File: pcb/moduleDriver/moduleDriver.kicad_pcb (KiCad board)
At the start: 2 copper layers, 72 x 80 mm, 56 parts, among them J1 MOTOR, J10 Sensor, J11 Power, J12 Power, J13 Power, J2 MOTOR, J3 MOTOR, J4 MOTOR, J5 IDC, J6 IDC, J7 Sensor, J8 Sensor, J9 Sensor, U1 TPIC6B595, U2 TPIC6B595, U3 74HC165, U4 74HC125, U5 PicoW, U6 OKI-78SR-5_1.5-W36-C, U8 74AHCT125

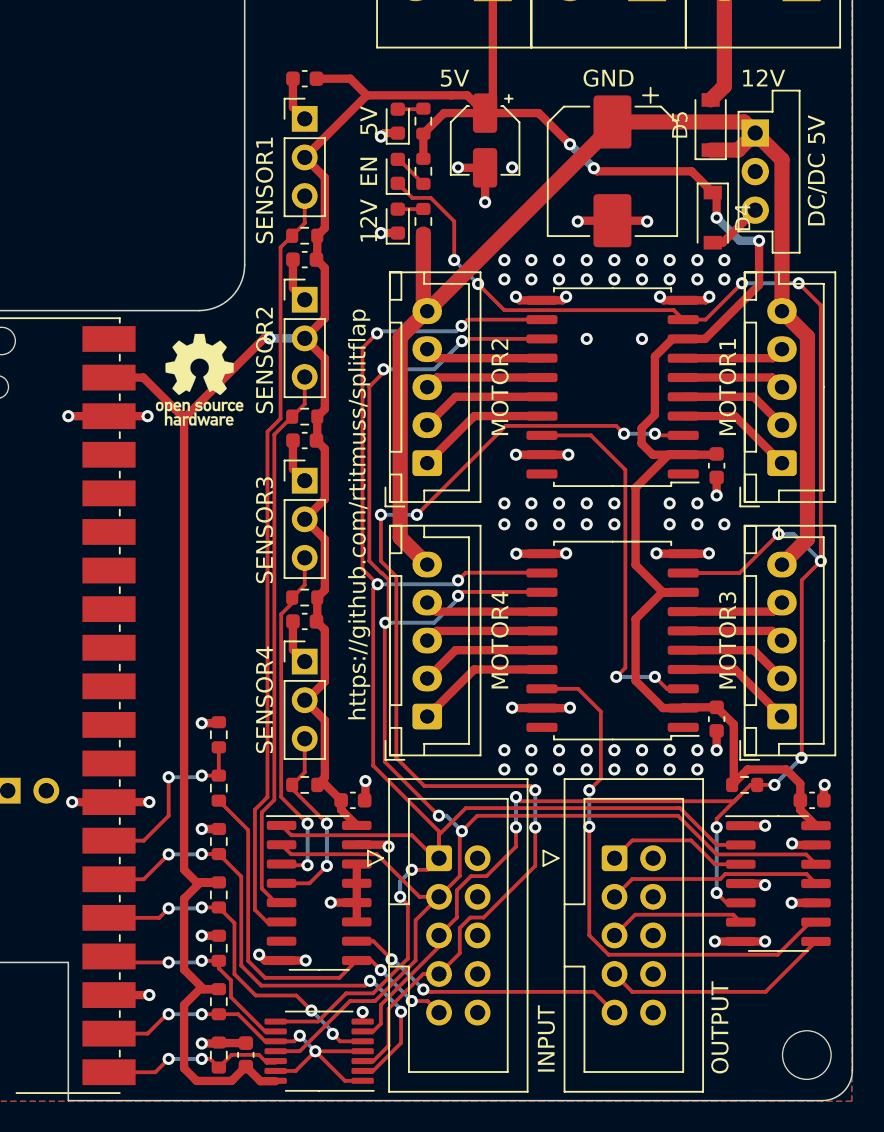
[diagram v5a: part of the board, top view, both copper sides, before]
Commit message: Iterate on level translation
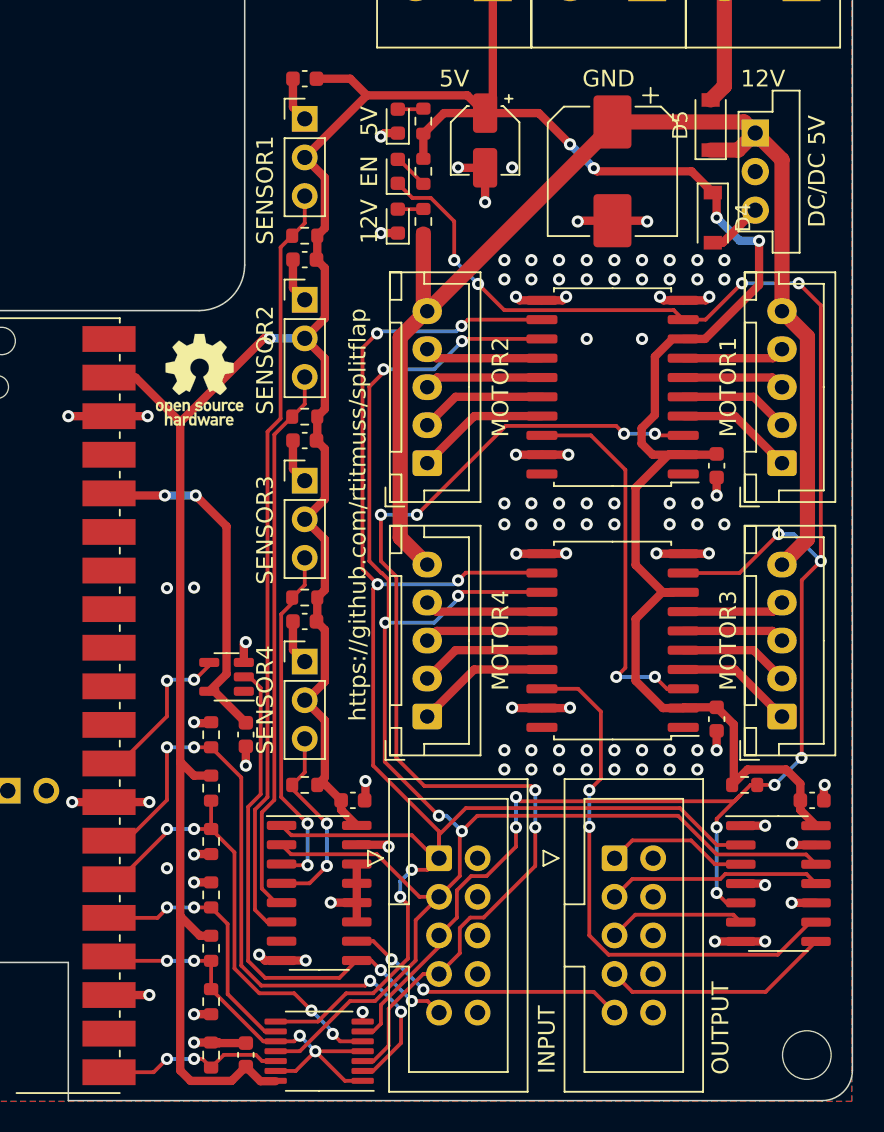
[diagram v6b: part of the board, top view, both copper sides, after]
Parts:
- removed R10: 2.4k, Resistor_SMD:R_0603_1608Metric
- removed R11: 1.2k, Resistor_SMD:R_0603_1608Metric
- added C8: 1uF, Capacitor_SMD:C_0603_1608Metric, F.Cu at (100.1, 105.9)
- added R16: 100k, Resistor_SMD:R_0603_1608Metric, F.Cu at (97.8, 112.9)
- added R17: 4.7k, Resistor_SMD:R_0603_1608Metric, F.Cu at (97.8, 123.5)
- added U7: SN74LVC1G04DBVR, Package_TO_SOT_SMD:SOT-23-5, F.Cu at (98.8, 102.1)
- R1: value 2.4k -> 2.2k
- R12, R9: value 100k -> 2.2k
- R15: value 100k -> 4.7k
- moved R15 17.6 mm to (97.8, 105.9), turned to -90 degrees
- moved R13 3.55 mm to (97.8, 116.5)
- moved R9 3.55 mm to (97.8, 120.0)
- moved R12 3.55 mm to (97.8, 109.4), turned to 90 degrees
- moved R4 0.51 mm to (97.8, 127.0)
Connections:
- R12 pad 1: GND -> /~{PWR_ENABLE_IN_3V3}
- R12 pad 2: /MOTOR_IN_3V3 -> +5V
- R15 pad 1: /~{BUFFER_ENABLE_3V3} -> GND
- R15 pad 2: +5V -> /MOTOR_IN_3V3
- R9 pad 1: /~{PWR_ENABLE_IN_3V3} -> /~{BUFFER_ENABLE_3V3}
- U5 pad 22: /~{BUFFER_ENABLE_3V3} -> unconnected-(U5-Pad22)
- U5 pad 24: /LATCH_IN_3V3 -> /~{BUFFER_ENABLE_3V3}
- U5 pad 25: /~{PWR_ENABLE_IN_3V3} -> /LATCH_IN_3V3
- U5 pad 26: /MOTOR_IN_3V3 -> /~{PWR_ENABLE_IN_3V3}
- U5 pad 27: /SENSOR_OUT_3V3 -> /MOTOR_IN_3V3
- U5 pad 29: unconnected-(U5-Pad29) -> /~{SENSOR_OUT_3V3}
- U5 pad 36: unconnected-(U5-Pad36) -> +3.3V
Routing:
- net +3.3V: track 0.00 -> 23.6 mm, vias 0 -> 2
- net /SENSOR_OUT_3V3: track 13.1 -> 0.00 mm, vias 2 -> 0
- net /~{SENSOR_OUT_3V3}: track 0.00 -> 10.1 mm, vias 0 -> 2
- net /MOTOR_IN_3V3: track 34.1 -> 42.6 mm
- net /SENSOR_OUT: track 26.3 -> 34.3 mm
- net /~{PWR_ENABLE_IN_3V3}: track 23.8 -> 29.8 mm
- net +5V: track 248.4 -> 244.4 mm
- net GND: track 108.5 -> 111.6 mm, vias 101 -> 107
- net /LATCH_IN_3V3: track 15.2 -> 18.3 mm
- net /~{BUFFER_ENABLE_3V3}: track 26.6 -> 28.3 mm
- net +12V: track 84.5 -> 83.8 mm

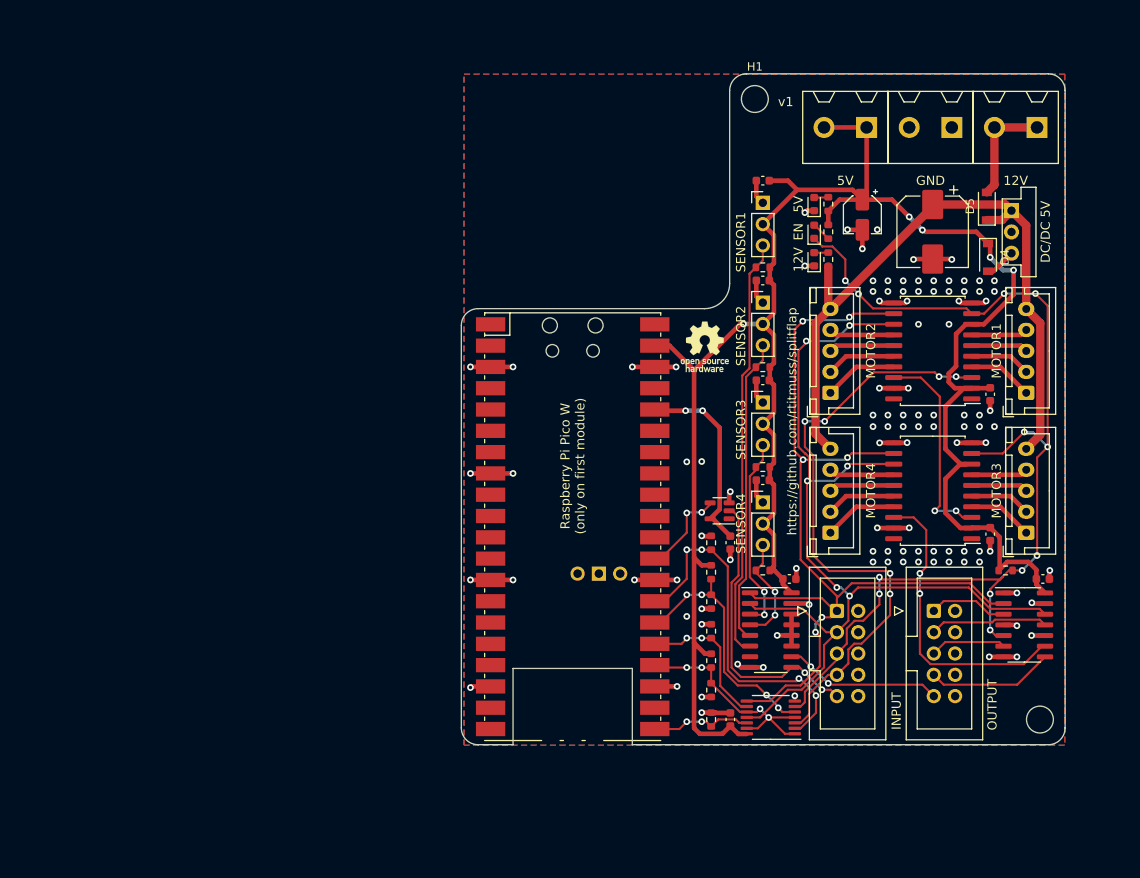
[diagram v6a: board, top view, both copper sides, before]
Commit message: Initial layout for new schematic
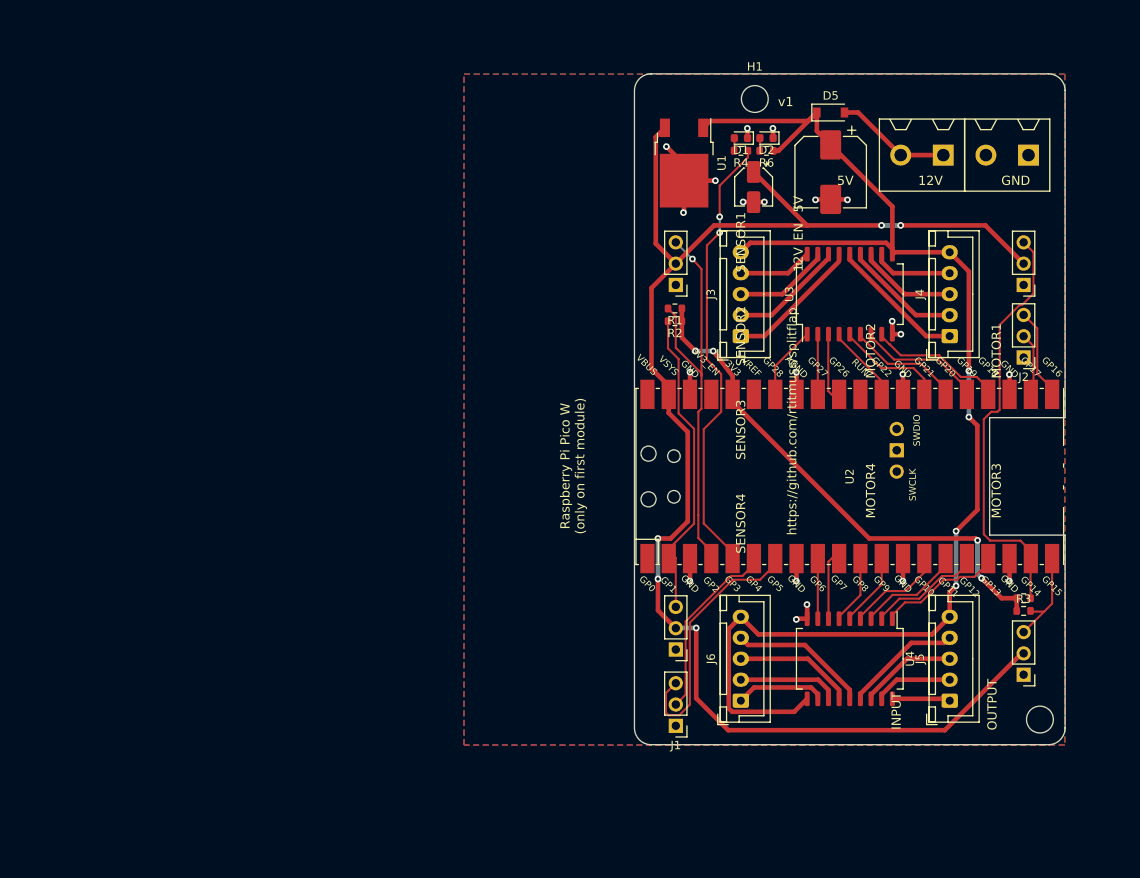
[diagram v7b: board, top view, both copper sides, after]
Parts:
- removed C10, C11, C12, C2, C3, C5, C6, C7, C8, C9: 1uF, Capacitor_SMD:C_0603_1608Metric
- removed D3: LED, LED_SMD:LED_0603_1608Metric
- removed D4: B5819W, Diode_SMD:D_SOD-123
- removed J13: Power, Library:ScrewTerminal-5.08-2P
- removed R12, R9: 2.2k, Resistor_SMD:R_0603_1608Metric
- removed R13, R14, R16: 100k, Resistor_SMD:R_0603_1608Metric
- removed R15, R17: 4.7k, Resistor_SMD:R_0603_1608Metric
- removed R8, locked: 47k, Resistor_SMD:R_0603_1608Metric
- removed REF**: OSHW-Logo_5.7x6mm_SilkScreen, Symbol:OSHW-Logo_5.7x6mm_SilkScreen
- removed U5: PicoW, Library:RPi_PicoW_SMD_TH
- removed U6: OKI-78SR-5_1.5-W36-C, Converter_DCDC:Converter_DCDC_Murata_OKI-78SR_Vertical
- removed U7: SN74LVC1G04DBVR, Package_TO_SOT_SMD:SOT-23-5
- removed U8: 74AHCT125, Package_SO:TSSOP-14_4.4x5mm_P0.65mm
- J1: value MOTOR -> UART_RL; footprint Connector_JST:JST_XH_B5B-XH-A_1x05_P2.50mm_Vertical -> Connector_PinHeader_2.54mm:PinHeader_1x03_P2.54mm_Vertical
- J2: value MOTOR -> UART_LR; footprint Connector_JST:JST_XH_B5B-XH-A_1x05_P2.50mm_Vertical -> Connector_PinHeader_2.54mm:PinHeader_1x03_P2.54mm_Vertical
- J5, J6: value IDC -> MOTOR; footprint Connector_IDC:IDC-Header_2x05_P2.54mm_Vertical -> Connector_JST:JST_XH_B5B-XH-A_1x05_P2.50mm_Vertical
- R1: value 2.2k -> 47k
- R2, R3: value 1.2k -> 47k
- R4: value 100k -> 1.2k
- R6: value 47k -> 2.2k
- U1: value TPIC6B595 -> MC7805BDTG; footprint Package_SO:SOIC-20W_7.5x12.8mm_P1.27mm -> Package_TO_SOT_SMD:TO-252-2
- U2: value TPIC6B595 -> PicoW; footprint Package_SO:SOIC-20W_7.5x12.8mm_P1.27mm -> Library:RPi_PicoW_SMD_TH
- U3: value 74HC165 -> ULN2803A; footprint Package_SO:SOIC-16_3.9x9.9mm_P1.27mm -> Package_SO:SOP-18_7x12.5mm_P1.27mm
- U4: value 74HC125 -> ULN2803A; footprint Package_SO:SOIC-14_3.9x8.7mm_P1.27mm -> Package_SO:SOP-18_7x12.5mm_P1.27mm
- moved R4 67.9 mm to (101.3, 59.2), turned to 180 degrees
- moved J1 57.6 mm to (93.6, 127.7), turned to 180 degrees
- moved R3 50.9 mm to (135.1, 114.0), turned to 0 degrees
- moved R5 50.2 mm to (135.1, 112.5), turned to 0 degrees
- moved J3 41.3 mm to (101.3, 81.3)
- moved U3 41.2 mm to (114.3, 76.3), turned to 90 degrees
- moved J10 37.3 mm to (135.1, 121.7), turned to 180 degrees
- moved U1 37.2 mm to (94.6, 60.6), turned to -90 degrees
- moved J7 32.6 mm to (135.1, 75.2), turned to 180 degrees
- moved J9 31.2 mm to (93.6, 118.7), turned to 180 degrees
- moved J4 27.4 mm to (126.2, 81.3)
- moved R6 25.8 mm to (104.4, 59.2)
- moved J6 25.4 mm to (101.3, 124.8), turned to 90 degrees
- moved J2 23.4 mm to (135.1, 83.8), turned to 180 degrees
- moved R2 23.0 mm to (93.5, 79.5), turned to 180 degrees
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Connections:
- J1 pad 1: /MOTOR_A_PHASE_A -> GND
- J1 pad 2: /MOTOR_A_PHASE_B -> /UART_RL_TX
- J1 pad 3: /MOTOR_A_PHASE_C -> /UART_RL_RX
- J2 pad 1: /MOTOR_B_PHASE_A -> GND
- J2 pad 2: /MOTOR_B_PHASE_B -> /UART_LR_RX
- J2 pad 3: /MOTOR_B_PHASE_C -> /UART_LR_TX
- J3 pad 1: /MOTOR_C_PHASE_A -> /MOTOR_A_PHASE_A
- J3 pad 2: /MOTOR_C_PHASE_B -> /MOTOR_A_PHASE_B
- J3 pad 3: /MOTOR_C_PHASE_C -> /MOTOR_A_PHASE_C
- J3 pad 4: /MOTOR_C_PHASE_D -> /MOTOR_A_PHASE_D
- J4 pad 1: /MOTOR_D_PHASE_A -> /MOTOR_B_PHASE_A
- J4 pad 2: /MOTOR_D_PHASE_B -> /MOTOR_B_PHASE_B
- J4 pad 3: /MOTOR_D_PHASE_C -> /MOTOR_B_PHASE_C
- J4 pad 4: /MOTOR_D_PHASE_D -> /MOTOR_B_PHASE_D
- J5 pad 1: /LATCH_IN -> /MOTOR_C_PHASE_A
- J5 pad 2: GND -> /MOTOR_C_PHASE_B
- J5 pad 3: /CLOCK_IN -> /MOTOR_C_PHASE_C
- J5 pad 4: GND -> /MOTOR_C_PHASE_D
- J5 pad 5: /~{PWR_ENABLE_IN} -> +12V
- J6 pad 1: /LATCH_OUT -> /MOTOR_D_PHASE_A
- J6 pad 2: GND -> /MOTOR_D_PHASE_B
- J6 pad 3: /CLOCK_OUT -> /MOTOR_D_PHASE_C
- J6 pad 4: GND -> /MOTOR_D_PHASE_D
- J6 pad 5: /~{PWR_ENABLE_OUT} -> +12V
- R1 pad 1: +12V -> +3.3V
- R1 pad 2: Net-(D1-Pad2) -> /SENSOR_B
- R2 pad 1: +5V -> +3.3V
- R2 pad 2: Net-(D2-Pad2) -> /SENSOR_C
- R3 pad 1: +5V -> +3.3V
- R3 pad 2: Net-(D3-Pad2) -> /SENSOR_D
- R4 pad 1: GND -> /LED
- R4 pad 2: /CLOCK_IN_3V3 -> Net-(D1-Pad2)
- R5 pad 1: +5V -> +3.3V
- R6 pad 1: +5V -> +12V
- R6 pad 2: /SENSOR_B -> Net-(D2-Pad2)
- U1 pad 1: unconnected-(U1-Pad1) -> +12V
- U1 pad 2: +5V -> GND
- U1 pad 3: /MOTOR_IN -> +5V
- U2 pad 10: GND -> /MOTOR_D_PHASE_C_P
- U2 pad 11: GND -> /MOTOR_D_PHASE_B_P
- U2 pad 12: /LATCH_IN -> /MOTOR_D_PHASE_A_P
- U2 pad 13: /CLOCK_IN -> GND
- U2 pad 14: /MOTOR_D_PHASE_D -> /MOTOR_C_PHASE_D_P
- U2 pad 15: /MOTOR_D_PHASE_C -> /MOTOR_C_PHASE_C_P
- U2 pad 16: /MOTOR_D_PHASE_B -> /MOTOR_C_PHASE_B_P
- U2 pad 17: /MOTOR_D_PHASE_A -> /MOTOR_C_PHASE_A_P
- U2 pad 18: /MOTOR_SER_OUT -> GND
- U2 pad 19: GND -> /SENSOR_A
- U2 pad 2: +5V -> /SENSOR_C
- U2 pad 20: unconnected-(U2-Pad20) -> /SENSOR_D
- U2 pad 3: Net-(U1-Pad18) -> GND
- U2 pad 4: /MOTOR_C_PHASE_A -> /SENSOR_B
- U2 pad 5: /MOTOR_C_PHASE_B -> /LED
- U2 pad 6: /MOTOR_C_PHASE_C -> /UART_RL_TX
- U2 pad 7: /MOTOR_C_PHASE_D -> /UART_RL_RX
- U2 pad 8: +5V -> GND
- U2 pad 9: /~{PWR_ENABLE_IN} -> /MOTOR_D_PHASE_D_P
- U3 pad 1: /LATCH_IN -> /MOTOR_A_PHASE_A_P
- U3 pad 10: /SENSOR_IN -> +12V
- U3 pad 11: GND -> /MOTOR_B_PHASE_D
- U3 pad 12: GND -> /MOTOR_B_PHASE_C
- U3 pad 13: GND -> /MOTOR_B_PHASE_B
- U3 pad 14: GND -> /MOTOR_B_PHASE_A
- U3 pad 15: GND -> /MOTOR_A_PHASE_A
- U3 pad 16: +5V -> /MOTOR_A_PHASE_B
- U3 pad 2: /CLOCK_IN -> /MOTOR_A_PHASE_B_P
- U3 pad 3: /SENSOR_C -> /MOTOR_A_PHASE_C_P
- U3 pad 4: /SENSOR_D -> /MOTOR_A_PHASE_D_P
- U3 pad 5: /SENSOR_B -> /MOTOR_B_PHASE_A_P
- U3 pad 6: /SENSOR_A -> /MOTOR_B_PHASE_B_P
- U3 pad 7: unconnected-(U3-Pad7) -> /MOTOR_B_PHASE_C_P
- U3 pad 8: GND -> /MOTOR_B_PHASE_D_P
- U3 pad 9: /SENSOR_OUT -> GND
- U4 pad 1: GND -> /MOTOR_C_PHASE_A_P
- U4 pad 10: GND -> +12V
- U4 pad 11: /CLOCK_OUT -> /MOTOR_D_PHASE_A
- U4 pad 12: /CLOCK_IN -> /MOTOR_D_PHASE_B
- U4 pad 13: GND -> /MOTOR_D_PHASE_C
- U4 pad 14: +5V -> /MOTOR_D_PHASE_D
- U4 pad 2: /LATCH_IN -> /MOTOR_C_PHASE_B_P
- U4 pad 3: /LATCH_OUT -> /MOTOR_C_PHASE_C_P
- U4 pad 4: GND -> /MOTOR_C_PHASE_D_P
- U4 pad 5: /~{PWR_ENABLE_IN} -> /MOTOR_D_PHASE_A_P
- U4 pad 6: /~{PWR_ENABLE_OUT} -> /MOTOR_D_PHASE_B_P
- U4 pad 7: GND -> /MOTOR_D_PHASE_C_P
- U4 pad 8: /MOTOR_OUT -> /MOTOR_D_PHASE_D_P
- U4 pad 9: /MOTOR_SER_OUT -> GND
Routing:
- net /~{PWR_ENABLE_IN}: track 125.4 -> 0.00 mm, vias 12 -> 0
- net /CLOCK_IN: track 114.6 -> 0.00 mm, vias 6 -> 0
- net /LATCH_IN: track 112.6 -> 0.00 mm, vias 6 -> 0
- net +12V: track 83.8 -> 162.9 mm, vias 0 -> 4
- net /MOTOR_IN: track 73.1 -> 0.00 mm, vias 6 -> 0
- net +5V: track 244.4 -> 177.0 mm
- net GND: track 111.6 -> 54.9 mm, vias 107 -> 21
- net /LED: track 0.00 -> 52.8 mm, vias 0 -> 2
- net /MOTOR_IN_3V3: track 42.6 -> 0.00 mm, vias 4 -> 0
- net +3.3V: track 23.6 -> 62.2 mm, vias 2 -> 4
- net /MOTOR_SER_OUT: track 35.1 -> 0.00 mm, vias 2 -> 0
- net /SENSOR_OUT: track 34.3 -> 0.00 mm, vias 2 -> 0
- net /UART_RL_RX: track 0.00 -> 31.9 mm
- net /~{PWR_ENABLE_IN_3V3}: track 29.8 -> 0.00 mm, vias 4 -> 0
- net /~{BUFFER_ENABLE_3V3}: track 28.3 -> 0.00 mm, vias 4 -> 0
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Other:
- board size 72 x 80 mm -> 51.4 x 80 mm
- board text removed: "DC/DC 5V"

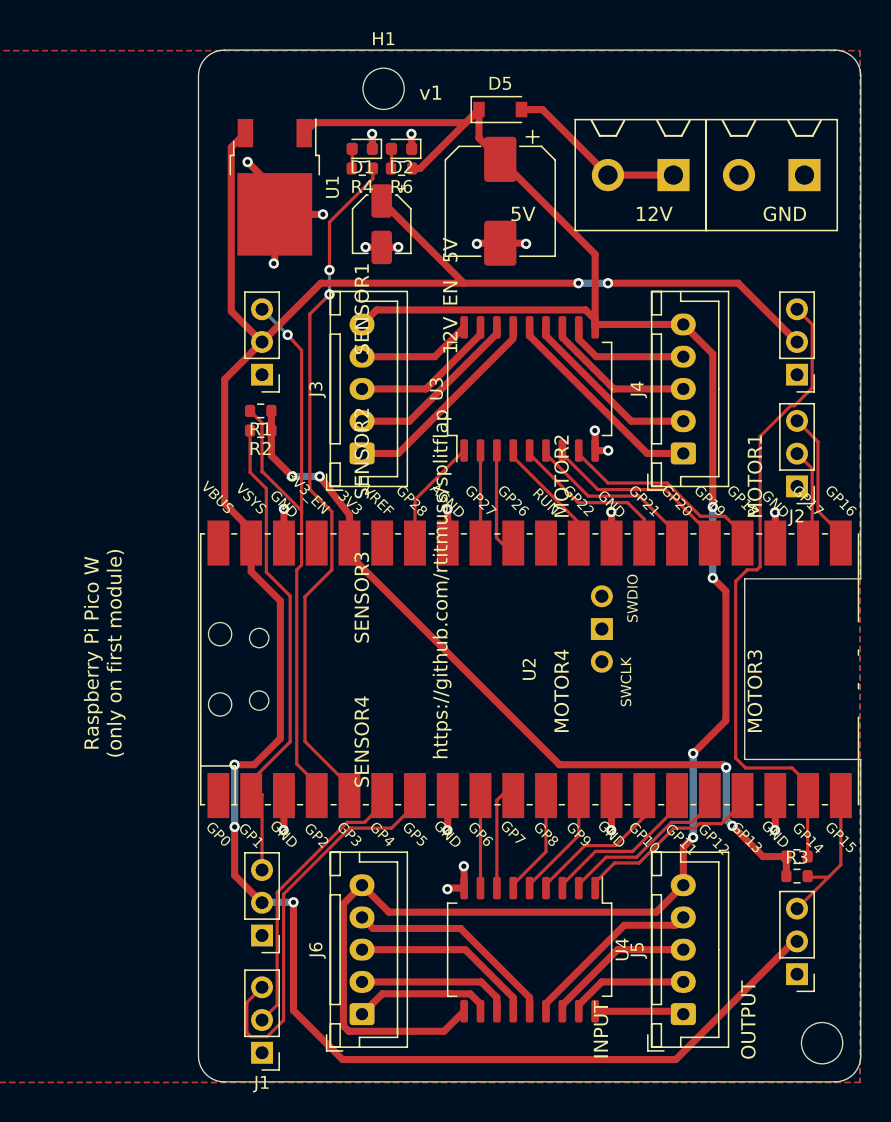
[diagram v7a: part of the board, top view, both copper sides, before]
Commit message: Add mounting holes and fix silkscreen
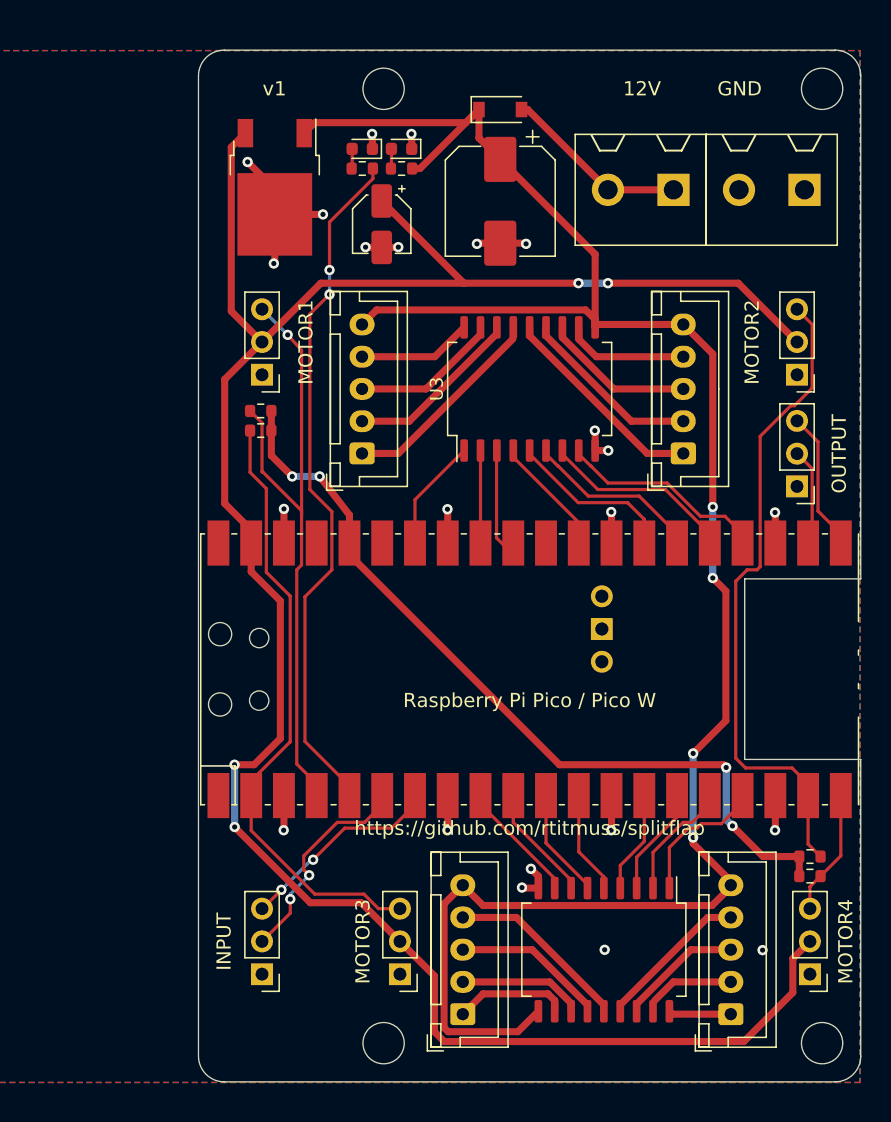
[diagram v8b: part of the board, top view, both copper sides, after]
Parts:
- added H2: MountingHole, MountingHole:MountingHole_3.2mm_M3_ISO7380, F.Cu at (103.0, 127.0)
- added H4: MountingHole, MountingHole:MountingHole_3.2mm_M3_ISO7380, F.Cu at (137.0, 53.0)
- moved QR***** 40.0 mm to (120.1, 119.8)
- moved QR***** 37.2 mm to (114.3, 76.3)
- moved J9 11.1 mm to (104.3, 121.7)
- moved J6 7.81 mm to (109.1, 124.8)
- moved J1 6.10 mm to (93.6, 121.7)
- moved U4 5.76 mm to (120.1, 119.8)
- moved J5 3.68 mm to (129.9, 124.8)
- moved J11 1.14 mm to (125.5, 60.8)
- moved J12 1.14 mm to (135.6, 60.8)
- moved J10 1.00 mm to (136.1, 121.7)
- moved R3 1.00 mm to (136.1, 114.0)
- moved R5 1.00 mm to (136.1, 112.5)
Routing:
- net /UART_RL_RX: track 31.9 -> 15.2 mm, vias 0 -> 2
- net /SENSOR_C: track 37.0 -> 47.4 mm
- net /UART_RL_TX: track 23.0 -> 16.0 mm, vias 0 -> 2
- net /MOTOR_C_PHASE_B_P: track 14.6 -> 8.71 mm
- net /MOTOR_C_PHASE_A_P: track 15.9 -> 10.3 mm
- net +12V: track 162.9 -> 157.6 mm
- net +5V: track 177.0 -> 171.8 mm, vias 5 -> 4
- net /MOTOR_C_PHASE_C_P: track 13.4 -> 9.37 mm
- net /MOTOR_C_PHASE_D_P: track 12.6 -> 8.85 mm
- net /MOTOR_A_PHASE_D_P: track 10.2 -> 7.18 mm
- net /MOTOR_D_PHASE_C: track 14.3 -> 11.4 mm
- net /MOTOR_D_PHASE_D: track 16.6 -> 13.7 mm
- net /MOTOR_C_PHASE_B: track 9.33 -> 6.63 mm
- net /MOTOR_C_PHASE_D: track 14.0 -> 11.5 mm
- net /MOTOR_C_PHASE_C: track 11.6 -> 9.18 mm
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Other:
- board text added: "Raspberry Pi Pico / Pico W"
- board text removed: "5V"
- board text removed: "EN"
- board text removed: "Raspberry Pi Pico W (only on first module)"
- board text removed: "SENSOR1"
- board text removed: "SENSOR2"
- board text removed: "SENSOR3"
- board text removed: "SENSOR4"
